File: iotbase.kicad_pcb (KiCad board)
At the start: 2 copper layers, 39.4 x 48.3 mm, 13 parts, among them J1 USB_C_Receptacle_USB2.0, SW1 SW_Push, SW2 SW_Push, U1 AMS1117-3.3, U2 STF202-22T1G, U3 ESP32-C3-WROOM-02

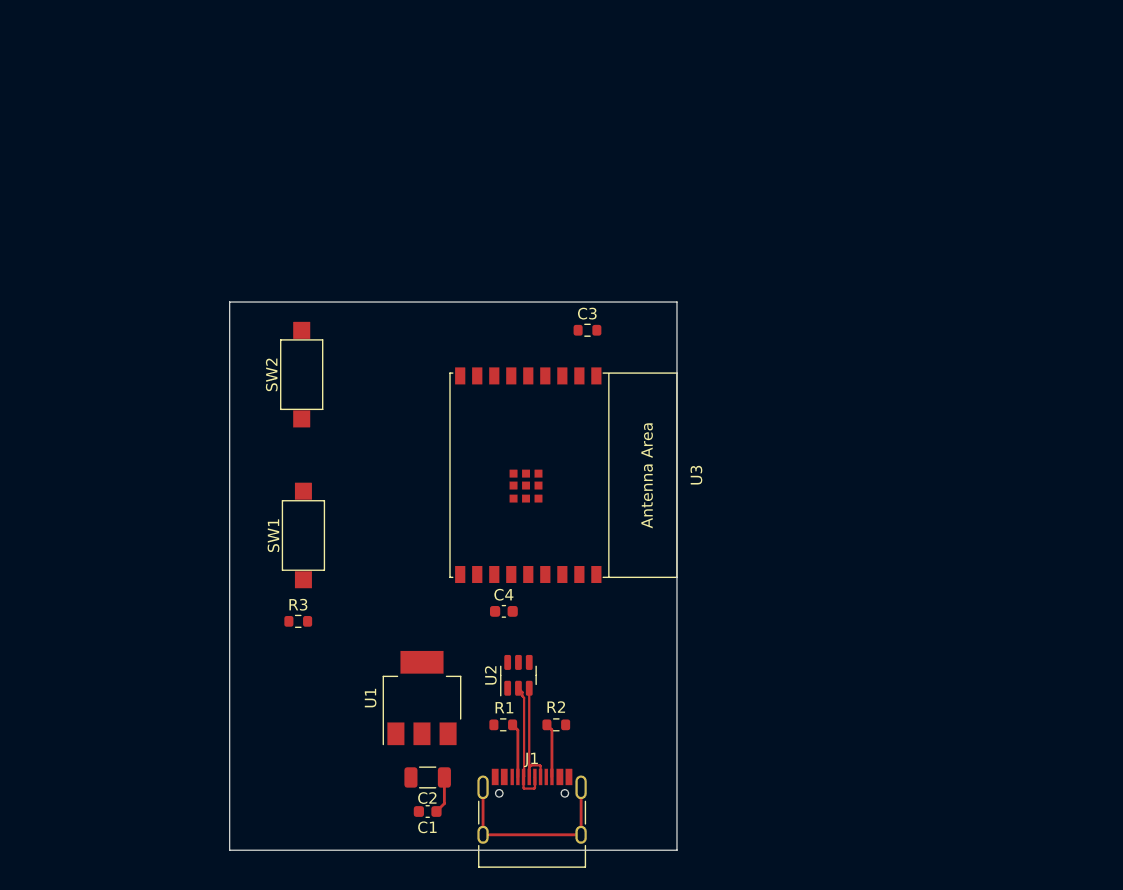
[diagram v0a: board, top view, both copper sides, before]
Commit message: adds additionals sensors and connectors
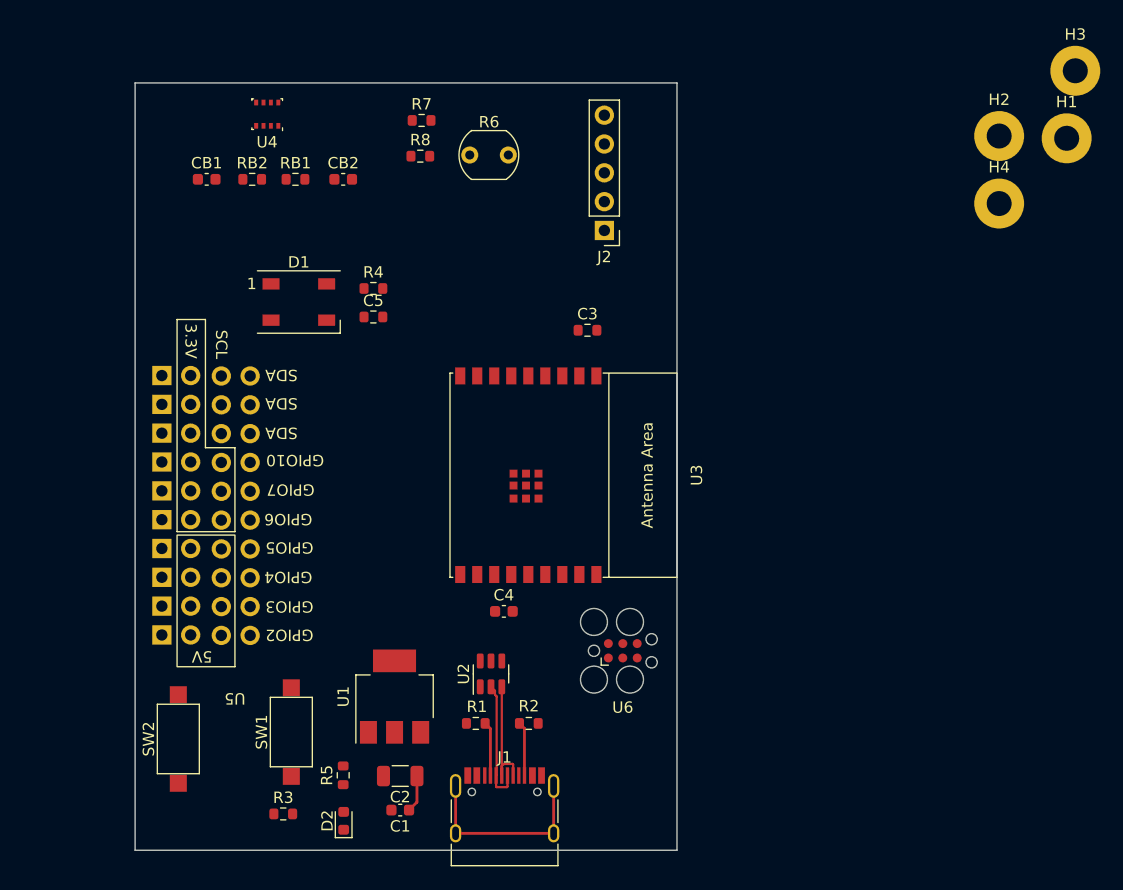
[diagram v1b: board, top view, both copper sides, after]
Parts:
- added C5: 10nF, Resistor_SMD:R_0603_1608Metric, F.Cu at (119.5, 83.1)
- added CB1: 100 nF, Capacitor_SMD:C_0603_1608Metric, F.Cu at (104.8, 70.9)
- added CB2: 100 nF, Capacitor_SMD:C_0603_1608Metric, F.Cu at (116.8, 70.9)
- added D1: WS2812B, LED_SMD:LED_WS2812B_PLCC4_5.0x5.0mm_P3.2mm, F.Cu at (112.9, 81.7)
- added D2: Power LED, LED_SMD:LED_0603_1608Metric, F.Cu at (116.9, 127.5)
- added H1: MountingHole_Pad, MountingHole:MountingHole_2.2mm_M2_Pad, F.Cu at (180.6, 67.3)
- added H2: MountingHole_Pad, MountingHole:MountingHole_2.2mm_M2_Pad, F.Cu at (174.6, 67.1)
- added H3: MountingHole_Pad, MountingHole:MountingHole_2.2mm_M2_Pad, F.Cu at (181.4, 61.4)
- added H4: MountingHole_Pad, MountingHole:MountingHole_2.2mm_M2_Pad, F.Cu at (174.6, 73.1)
- added J2: RCWL-0516, Connector_PinHeader_2.54mm:PinHeader_1x05_P2.54mm_Vertical, F.Cu at (139.9, 75.4)
- added R4: 500 Ω, Resistor_SMD:R_0603_1608Metric, F.Cu at (119.5, 80.5)
- added R5: 5.1kΩ, Resistor_SMD:R_0603_1608Metric, F.Cu at (116.8, 123.4)
- added R6: LDR07, OptoDevice:R_LDR_5.1x4.3mm_P3.4mm_Vertical, F.Cu at (128.0, 68.8)
- added R7: 10kΩ, Resistor_SMD:R_0603_1608Metric, F.Cu at (123.7, 65.7)
- added R8: 10kΩ, Resistor_SMD:R_0603_1608Metric, F.Cu at (123.6, 68.9)
- added RB1: 4.7 K, Resistor_SMD:R_0603_1608Metric, F.Cu at (112.6, 70.9)
- added RB2: 4.7 K, Resistor_SMD:R_0603_1608Metric, F.Cu at (108.8, 70.9)
- added U4: BME280, Package_LGA:Bosch_LGA-8_2.5x2.5mm_P0.65mm_ClockwisePinNumbering, F.Cu at (110.1, 65.2)
- added U5: GPIO Connector, 0_my_library:Connector_IoT_GPIO, F.Cu at (107.3, 116.2)
- added U6: Connector_ESProg, Connector:Tag-Connect_TC2030-IDC-FP_2x03_P1.27mm_Vertical, F.Cu at (141.5, 112.5)
- SW1: value SW_Push -> Reset
- SW2: value SW_Push -> Boot
- moved SW2 33.9 mm to (102.3, 120.2)
- moved SW1 17.4 mm to (112.3, 119.6)
- moved R3 17.0 mm to (111.6, 126.8)
- moved R2 2.42 mm to (133.2, 118.9)
- moved J1 2.42 mm to (131.1, 127.5)
- moved R1 2.42 mm to (128.5, 118.9)
- moved C1 2.42 mm to (121.9, 126.5)
- moved C2 2.42 mm to (121.9, 123.5)
- moved U1 2.42 mm to (121.4, 116.5)
- moved U2 2.42 mm to (129.9, 114.5)
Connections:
- U3 pad 11: GPIO20 -> RXD
- U3 pad 12: GPIO21 -> TXD
- U3 pad 17: GPIO1 -> SCL
- U3 pad 18: GPIO0 -> SDA
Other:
- board size 39.4 x 48.3 mm -> 47.8 x 67.6 mm

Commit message: renames symbol and footprint libraries
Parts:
- U5: footprint 0_my_library:Connector_IoT_GPIO -> 0_Project:Connector_IoT_GPIO
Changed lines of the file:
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@@
     )
   )
-  (footprint "0_my_library:Connector_IoT_GPIO" (layer "F.Cu")
+  (footprint "0_Project:Connector_IoT_GPIO" (layer "F.Cu")
     (at 107.2996 116.177 180)
     (property "Sheetfile" "iotbase.kicad_sch")

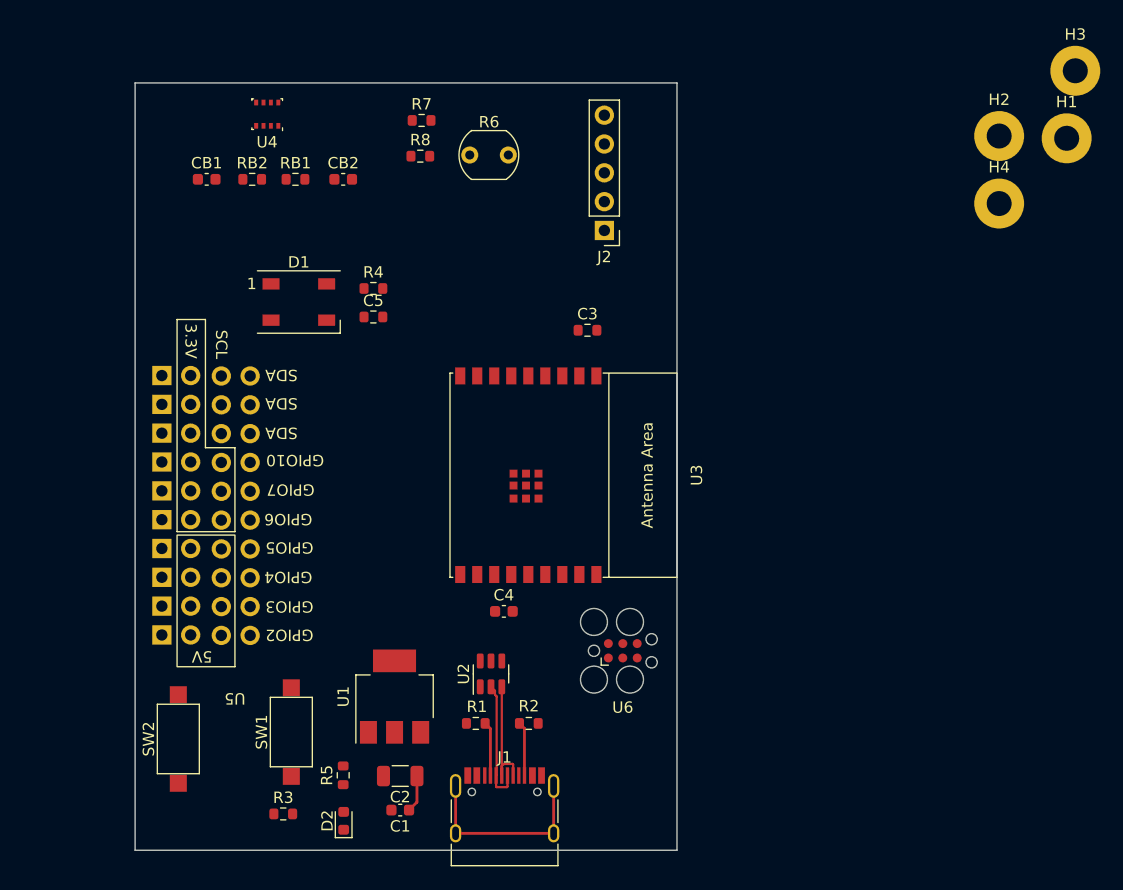
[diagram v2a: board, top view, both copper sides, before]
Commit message: updates board layout adds header for RCWL-0516 updates readme
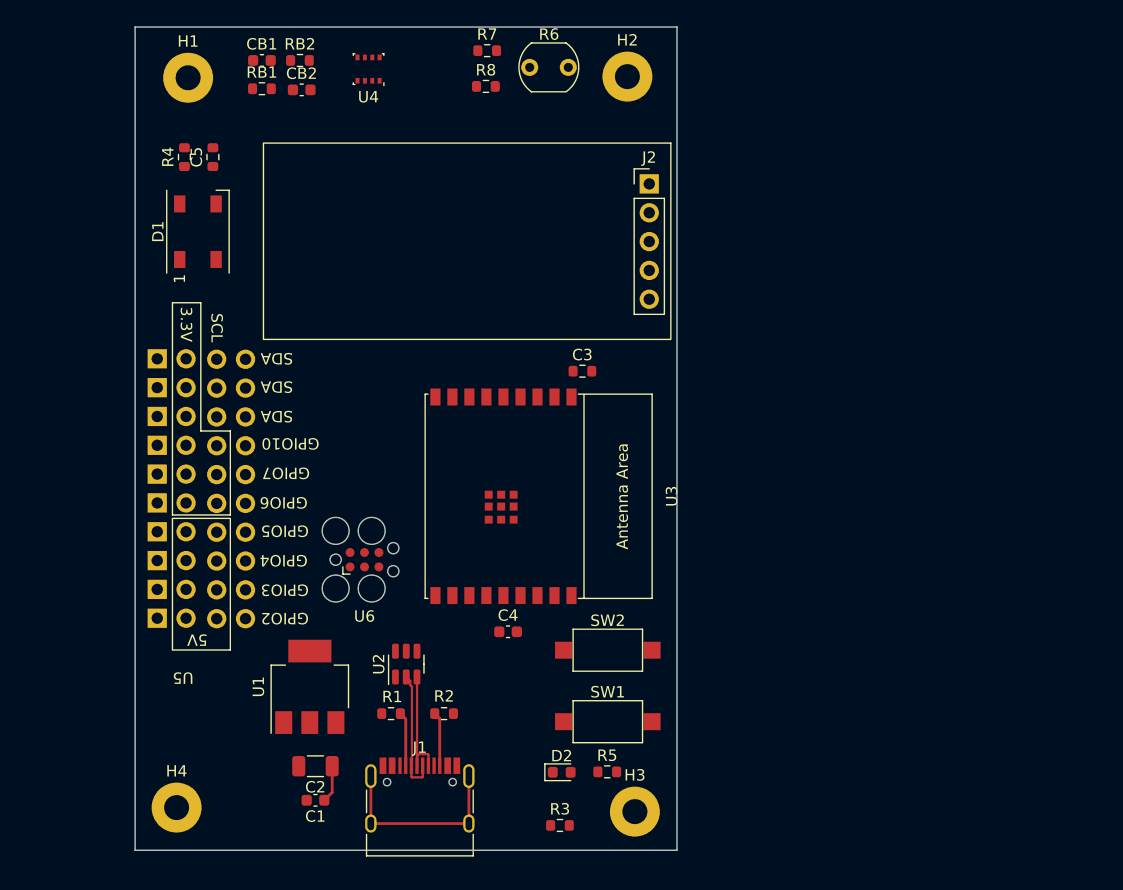
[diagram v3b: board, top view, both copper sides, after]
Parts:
- J2: footprint Connector_PinHeader_2.54mm:PinHeader_1x05_P2.54mm_Vertical -> 0_Project:PinHeader_RCWL-0516
- moved H4 89.9 mm to (102.2, 126.3)
- moved H1 77.6 mm to (103.2, 62.0)
- moved H3 75.9 mm to (142.5, 126.6)
- moved SW2 38.6 mm to (140.2, 112.4), turned to 0 degrees
- moved H2 33.2 mm to (141.9, 61.9)
- moved SW1 27.9 mm to (140.2, 118.7), turned to 0 degrees
- moved R3 24.4 mm to (135.9, 127.9)
- moved U6 24.1 mm to (118.7, 104.4)
- moved R5 23.3 mm to (140.1, 123.1), turned to 0 degrees
- moved R4 20.3 mm to (102.8, 69.0), turned to 90 degrees
- moved C5 20.0 mm to (105.4, 69.0), turned to 90 degrees
- moved D2 19.7 mm to (136.1, 123.2), turned to 0 degrees
- moved CB1 11.5 mm to (109.7, 60.5)
- moved RB2 11.3 mm to (113.0, 60.5)
- moved D1 10.8 mm to (104.0, 75.5), turned to 90 degrees
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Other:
- board size 47.8 x 67.6 mm -> 47.8 x 72.5 mm

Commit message: routing and repositioning
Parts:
- moved R3 41.1 mm to (136.2, 86.7), turned to 180 degrees
- moved C4 16.3 mm to (115.1, 110.2)
- moved R4 9.36 mm to (106.3, 77.7), turned to 180 degrees
- moved C5 9.09 mm to (102.8, 77.7), turned to 0 degrees
- moved SW2 6.68 mm to (134.6, 116.1), turned to 180 degrees
- moved SW1 6.32 mm to (134.6, 121.8), turned to 180 degrees
- moved R5 5.83 mm to (136.0, 127.3)
- moved D2 5.83 mm to (132.0, 127.4)
- moved C3 5.50 mm to (132.5, 86.7), turned to 180 degrees
- moved C2 3.17 mm to (111.6, 124.1), turned to -90 degrees
- moved D1 2.64 mm to (104.0, 72.9)
- moved U3 2.00 mm to (133.5, 100.7)
- moved C1 1.70 mm to (115.1, 124.1), turned to -90 degrees
- moved R2 0.98 mm to (124.8, 118.2)
- moved J1 0.98 mm to (122.6, 126.8)
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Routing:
- net SCL: track 0.00 -> 49.9 mm, vias 0 -> 2
- net SDA: track 0.00 -> 48.7 mm, vias 0 -> 2
- net VBUS: track 3.29 -> 44.2 mm, vias 0 -> 2
- net GPIO4: track 0.00 -> 31.9 mm
- net GPIO8: track 0.00 -> 31.2 mm
- net GPIO5: track 0.00 -> 29.3 mm
- net GPIO6: track 0.00 -> 26.7 mm
- net GPIO7: track 0.00 -> 24.1 mm
- net BOOT: track 0.00 -> 16.6 mm, vias 0 -> 2
- net +3V3: track 0.00 -> 14.4 mm, vias 0 -> 1
- net TXD: track 0.00 -> 14.4 mm
- net EN: track 0.00 -> 14.1 mm, vias 0 -> 1
- net GND: track 0.00 -> 12.0 mm
- net RXD: track 0.00 -> 11.5 mm
- net D-: track 0.00 -> 11.2 mm
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- added copper zone on F.Cu, net GND

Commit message: additional routing
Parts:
- moved R8 50.0 mm to (135.0, 112.5)
- moved R5 30.2 mm to (106.1, 123.1), turned to 90 degrees
- moved D2 27.2 mm to (106.1, 119.1), turned to -90 degrees
- moved CB2 7.47 mm to (120.3, 65.2)
- moved RB1 6.35 mm to (115.7, 65.0)
- moved U4 1.36 mm to (118.3, 60.1)
- moved RB2 1.34 mm to (114.4, 60.2), turned to 90 degrees
- moved J2 0.90 mm to (143.1, 70.8)
- moved SW2 0.11 mm to (134.6, 116.0)
- moved SW1 0.10 mm to (134.6, 121.9)
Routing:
- net EN: track 14.1 -> 51.6 mm, vias 1 -> 3
- net +3V3: track 14.4 -> 48.0 mm
- net GPIO8: track 31.2 -> 1.49 mm
- net SDA: track 48.7 -> 76.5 mm
- net BOOT: track 16.6 -> 41.1 mm, vias 2 -> 3
- net SCL: track 49.9 -> 52.9 mm
- net Net-(D2-Pad2): track 0.00 -> 2.41 mm

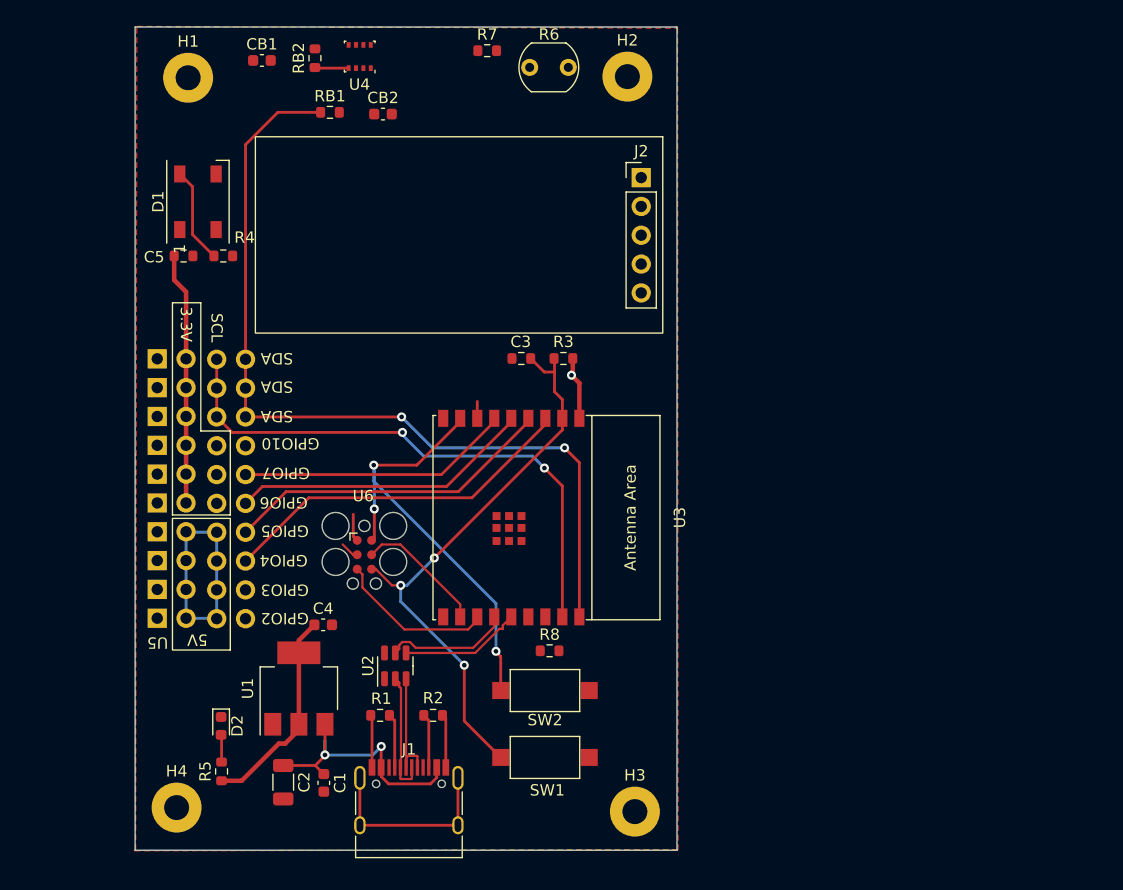
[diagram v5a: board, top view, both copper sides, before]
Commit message: updates gpio connector adds additional traces adds jlcpcb fab plugin
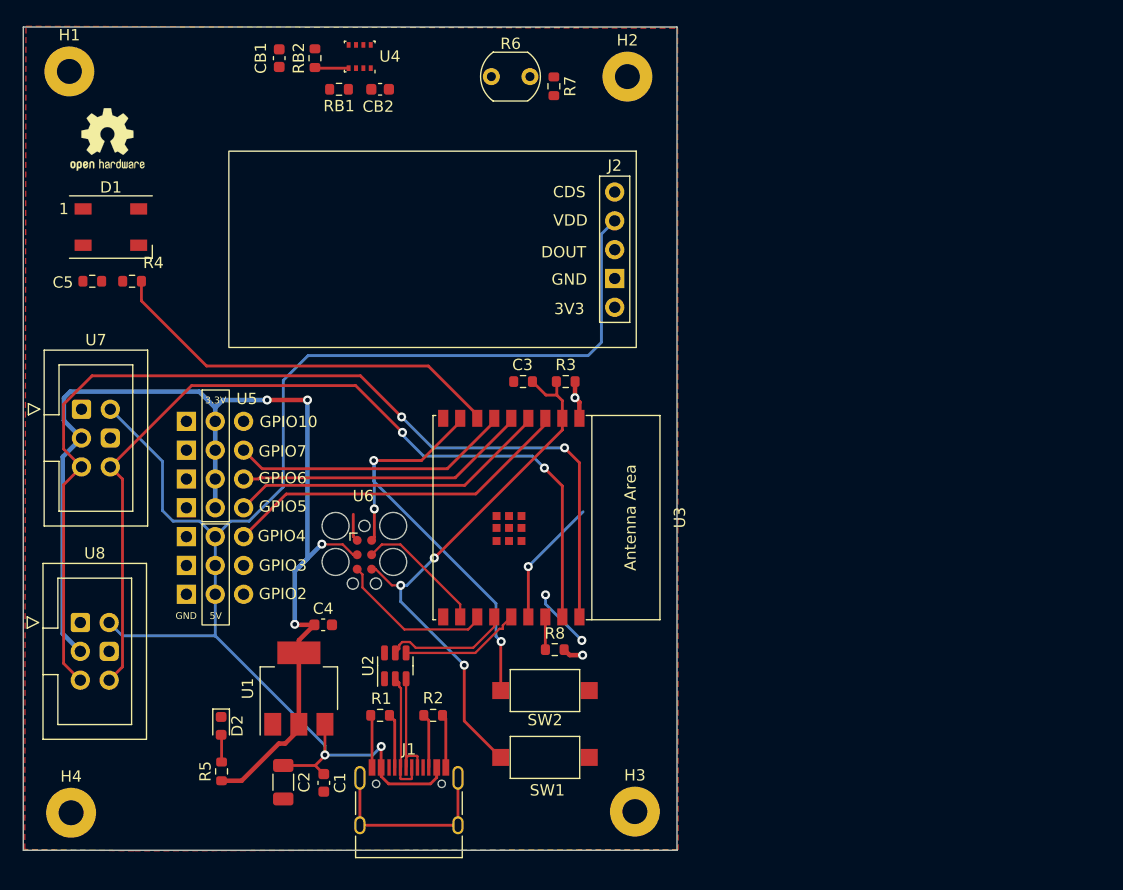
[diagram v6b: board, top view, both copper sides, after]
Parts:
- added REF**: OSHW-Logo2_7.3x6mm_SilkScreen, Symbol:OSHW-Logo2_7.3x6mm_SilkScreen, F.Cu at (96.1, 67.4)
- added U7: Connector_I2C, 0_Project:IDC-Header_2x03_P2.54mm_I2C, F.Cu at (93.8, 91.2)
- added U8: Connector_I2C, 0_Project:IDC-Header_2x03_P2.54mm_I2C, F.Cu at (93.7, 110.0)
- C5: value 10nF -> 100nF
- moved U5 27.6 mm to (109.4, 87.2), turned to 0 degrees
- moved H1 10.5 mm to (92.7, 61.4)
- moved H4 9.31 mm to (92.9, 126.7)
- moved C5 8.34 mm to (94.7, 79.9)
- moved R4 8.34 mm to (98.2, 79.9)
- moved D1 7.99 mm to (96.4, 75.1), turned to 0 degrees
- moved R7 6.66 mm to (135.4, 62.7), turned to -90 degrees
- moved R6 3.48 mm to (129.9, 61.9)
- moved J2 2.66 mm to (140.8, 72.0)
- moved CB2 2.20 mm to (120.1, 63.0)
- moved RB1 2.18 mm to (116.5, 63.0), turned to 180 degrees
- moved R3 2.04 mm to (136.4, 88.7)
- moved C3 2.04 mm to (132.7, 88.7)
- moved CB1 1.54 mm to (111.2, 60.2), turned to -90 degrees
- moved R8 0.47 mm to (135.5, 112.4)
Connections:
- C5 pad 1: +3V3 -> VBUS
- D1 pad 1: +3V3 -> VBUS
- J2 pad 2: GND -> VBUS
- J2 pad 4: VBUS -> GND
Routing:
- net VBUS: track 44.2 -> 129.5 mm
- net +3V3: track 48.0 -> 108.1 mm, vias 1 -> 6
- net GPIO8: track 1.49 -> 35.8 mm
- net SCL: track 52.9 -> 81.0 mm
- net SDA: track 76.5 -> 89.5 mm
- net GPIO3: track 0.00 -> 11.3 mm, vias 0 -> 1
- net Net-(D1-Pad4): track 8.47 -> 0.00 mm
- net GND: track 12.0 -> 17.3 mm, vias 0 -> 2
- net GPIO2: track 0.00 -> 2.89 mm
- net EN: track 51.6 -> 49.5 mm
- net GPIO4: track 31.9 -> 31.2 mm
- net GPIO5: track 29.3 -> 28.5 mm
- net BOOT: track 41.1 -> 41.8 mm
- net GPIO7: track 24.1 -> 24.8 mm
- net GPIO6: track 26.7 -> 26.1 mm
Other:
- board size 47.8 x 72.5 mm -> 57.6 x 72.5 mm
